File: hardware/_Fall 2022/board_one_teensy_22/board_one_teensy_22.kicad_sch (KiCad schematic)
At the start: 11 parts, among them J1 Conn_01x04, U1 Teensy4.1, U2 BNO055_Breakout, U3 MPL3115A2_Breakout

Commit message: Update main teensy board
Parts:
- added C1: 0.1uF, symbol Device:C
- R1, R2, R3: renamed from R?; value R -> 750
- gave numbers to parts that had none: 4
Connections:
- net GND: now also C1.2
- net Reg. 3.3 V renamed V_TEENSY
- net V_TEENSY: now also C1.1
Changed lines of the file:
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@@
+    (stroke (width 0) (type default) (color 0 0 0 0))
+  )
+  (wire (pts (xy 266.7 71.12) (xy 266.7 77.47))
     (stroke (width 0) (type default) (color 0 0 0 0))
   )
@@
     (stroke (width 0) (type default) (color 0 0 0 0))
   )
+  (wire (pts (xy 267.97 53.34) (xy 267.97 57.15))
+    (stroke (width 0) (type default) (color 0 0 0 0))
+  )
   (wire (pts (xy 88.9 180.34) (xy 100.33 180.34))
     (stroke (width 0) (type default) (color 0 0 0 0))
@@
     (stroke (width 0) (type default) (color 0 0 0 0))
   )
+  (wire (pts (xy 267.97 41.91) (xy 267.97 45.72))
+    (stroke (width 0) (type default) (color 0 0 0 0))
+  )
   (wire (pts (xy 22.86 35.56) (xy 35.56 35.56))
     (stroke (width 0) (type default) (color 0 0 0 0))
@@
     (effects (font (size 1.27 1.27)) (justify left bottom))
   )
+  (label "V_TEENSY" (at 267.97 41.91 0)
+    (effects (font (size 1.27 1.27)) (justify left bottom))
+  )
   (label "GND" (at 87.63 63.5 0)
     (effects (font (size 1.27 1.27)) (justify left bottom))
@@
     (effects (font (size 1.27 1.27)) (justify left bottom))
   )
-  (label "Reg. 3.3 V" (at 243.84 52.07 0)
+  (label "V_TEENSY" (at 243.84 52.07 0)
     (effects (font (size 1.27 1.27)) (justify left bottom))
   )
@@
   )
   (label "SCL0" (at 88.9 121.92 0)
+    (effects (font (size 1.27 1.27)) (justify left bottom))
+  )
+  (label "GND" (at 266.7 71.12 0)
     (effects (font (size 1.27 1.27)) (justify left bottom))
   )
@@
     (pin "4")
   )
+  (symbol (lib_id "power:GND") (at 266.7 77.47 0) (unit 1)
+    (in_bom yes) (on_board yes) (fields_autoplaced)
+    (property "Reference" "#PWR0102" (id 0) (at 266.7 83.82 0)
+      (effects (font (size 1.27 1.27)) hide)
+    )
+    (property "Value" "GND" (id 1) (at 266.7 82.55 0))
+    (property "Footprint" "" (id 2) (at 266.7 77.47 0)
+      (effects (font (size 1.27 1.27)) hide)
+    )
+    (property "Datasheet" "" (id 3) (at 266.7 77.47 0)
+      (effects (font (size 1.27 1.27)) hide)
+    )
+    (pin "1")
+  )
   (symbol (lib_id "REV2_SPRING_2022-rescue:MPL3115A2_Breakout-Sensors_2021_2022") (at 102.87 114.3 0) (unit 1)
     (in_bom yes) (on_board yes)
@@
   (symbol (lib_id "Connector:Conn_01x09_Female") (at 40.64 40.64 0) (unit 1)
     (in_bom yes) (on_board yes) (fields_autoplaced)
-    (property "Reference" "J?" (id 0) (at 41.91 39.3699 0)
+    (property "Reference" "J2" (id 0) (at 41.91 39.3699 0)
       (effects (font (size 1.27 1.27)) (justify left))
     )
@@
     (pin "9")
   )
+  (symbol (lib_id "power:GND") (at 267.97 57.15 0) (unit 1)
+    (in_bom yes) (on_board yes) (fields_autoplaced)
+    (property "Reference" "#PWR0101" (id 0) (at 267.97 63.5 0)
+      (effects (font (size 1.27 1.27)) hide)
+    )
+    (property "Value" "GND" (id 1) (at 267.97 62.23 0))
+    (property "Footprint" "" (id 2) (at 267.97 57.15 0)
+      (effects (font (size 1.27 1.27)) hide)
+    )
+    (property "Datasheet" "" (id 3) (at 267.97 57.15 0)
+      (effects (font (size 1.27 1.27)) hide)
+    )
+    (pin "1")
+  )
   (symbol (lib_id "Device:R") (at 85.09 157.48 90) (unit 1)
     (in_bom yes) (on_board yes) (fields_autoplaced)
-    (property "Reference" "R?" (id 0) (at 85.09 151.13 90))
-    (property "Value" "R" (id 1) (at 85.09 153.67 90))
+    (property "Reference" "R1" (id 0) (at 85.09 151.13 90))
+    (property "Value" "750" (id 1) (at 85.09 153.67 90))
     (property "Footprint" "" (id 2) (at 85.09 159.258 90)
       (effects (font (size 1.27 1.27)) hide)
@@
   (symbol (lib_id "Device:LED") (at 104.14 168.91 0) (unit 1)
     (in_bom yes) (on_board yes) (fields_autoplaced)
-    (property "Reference" "D?" (id 0) (at 102.5525 162.56 0))
+    (property "Reference" "D2" (id 0) (at 102.5525 162.56 0))
     (property "Value" "LED" (id 1) (at 102.5525 165.1 0))
     (property "Footprint" "" (id 2) (at 104.14 168.91 0)
@@
   (symbol (lib_id "Device:R") (at 85.09 180.34 90) (unit 1)
     (in_bom yes) (on_board yes) (fields_autoplaced)
-    (property "Reference" "R?" (id 0) (at 85.09 173.99 90))
-    (property "Value" "R" (id 1) (at 85.09 176.53 90))
+    (property "Reference" "R3" (id 0) (at 85.09 173.99 90))
+    (property "Value" "750" (id 1) (at 85.09 176.53 90))
     (property "Footprint" "" (id 2) (at 85.09 182.118 90)
       (effects (font (size 1.27 1.27)) hide)
@@
     (pin "4")
   )
+  (symbol (lib_id "Device:C") (at 267.97 49.53 0) (unit 1)
+    (in_bom yes) (on_board yes) (fields_autoplaced)
+    (property "Reference" "C1" (id 0) (at 271.78 48.2599 0)
+      (effects (font (size 1.27 1.27)) (justify left))
+    )
+    (property "Value" "0.1uF" (id 1) (at 271.78 50.7999 0)
+      (effects (font (size 1.27 1.27)) (justify left))
+    )
+    (property "Footprint" "" (id 2) (at 268.9352 53.34 0)
+      (effects (font (size 1.27 1.27)) hide)
+    )
+    (property "Datasheet" "~" (id 3) (at 267.97 49.53 0)
+      (effects (font (size 1.27 1.27)) hide)
+    )
+    (pin "1")
+    (pin "2")
+  )
   (symbol (lib_id "Device:LED") (at 104.14 180.34 0) (unit 1)
     (in_bom yes) (on_board yes) (fields_autoplaced)
-    (property "Reference" "D?" (id 0) (at 102.5525 173.99 0))
+    (property "Reference" "D3" (id 0) (at 102.5525 173.99 0))
     (property "Value" "LED" (id 1) (at 102.5525 176.53 0))
     (property "Footprint" "" (id 2) (at 104.14 180.34 0)
@@
   (symbol (lib_id "Device:LED") (at 104.14 157.48 0) (unit 1)
     (in_bom yes) (on_board yes) (fields_autoplaced)
-    (property "Reference" "D?" (id 0) (at 102.5525 151.13 0))
+    (property "Reference" "D1" (id 0) (at 102.5525 151.13 0))
     (property "Value" "LED" (id 1) (at 102.5525 153.67 0))
     (property "Footprint" "" (id 2) (at 104.14 157.48 0)
@@
   (symbol (lib_id "Device:R") (at 85.09 168.91 90) (unit 1)
     (in_bom yes) (on_board yes) (fields_autoplaced)
-    (property "Reference" "R?" (id 0) (at 85.09 162.56 90))
-    (property "Value" "R" (id 1) (at 85.09 165.1 90))
+    (property "Reference" "R2" (id 0) (at 85.09 162.56 90))
+    (property "Value" "750" (id 1) (at 85.09 165.1 90))
     (property "Footprint" "" (id 2) (at 85.09 170.688 90)
       (effects (font (size 1.27 1.27)) hide)
@@
   )
   (symbol_instances
+    (path "/8f40d9eb-5fdf-45db-bc50-610230c043b9"
+      (reference "#PWR0101") (unit 1) (value "GND") (footprint "")
+    )
+    (path "/46273ce1-7651-40e9-8fe5-ad122a75d0a7"
+      (reference "#PWR0102") (unit 1) (value "GND") (footprint "")
+    )
+    (path "/c535219e-946a-4ec5-bf45-7e1cca9e717d"
+      (reference "C1") (unit 1) (value "0.1uF") (footprint "")
+    )
+    (path "/e90f50d6-0a2f-4af0-9f06-35ce626c0dd6"
+      (reference "D1") (unit 1) (value "LED") (footprint "")
+    )
     (path "/ac0e113a-035a-46d2-97ae-1c57b8941c5b"
-      (reference "D?") (unit 1) (value "LED") (footprint "")
+      (reference "D2") (unit 1) (value "LED") (footprint "")
     )
     (path "/e2c8cf26-3d78-44d0-8af4-f027e582a996"
-      (reference "D?") (unit 1) (value "LED") (footprint "")
-    )
-    (path "/e90f50d6-0a2f-4af0-9f06-35ce626c0dd6"
-      (reference "D?") (unit 1) (value "LED") (footprint "")
+      (reference "D3") (unit 1) (value "LED") (footprint "")
     )
     (path "/c1ad9257-9aae-4dda-b1f1-b68d34349218"
@@
     )
     (path "/8786a6df-54d0-499d-9a7d-c5f993b94e72"
-      (reference "J?") (unit 1) (value "Conn_01x09_Female") (footprint "")
+      (reference "J2") (unit 1) (value "Conn_01x09_Female") (footprint "")
     )
     (path "/93bdb61a-71f4-45c4-b1f5-96e6332b02ef"
-      (reference "R?") (unit 1) (value "R") (footprint "")
+      (reference "R1") (unit 1) (value "750") (footprint "")
+    )
+    (path "/e9dd9e52-6e0d-4182-9ca4-63d8a2882b48"
+      (reference "R2") (unit 1) (value "750") (footprint "")
     )
     (path "/aca13756-ff3c-44cf-93bb-52afba450064"
-      (reference "R?") (unit 1) (value "R") (footprint "")
-    )
-    (path "/e9dd9e52-6e0d-4182-9ca4-63d8a2882b48"
-      (reference "R?") (unit 1) (value "R") (footprint "")
+      (reference "R3") (unit 1) (value "750") (footprint "")
     )
     (path "/1049841c-d8e6-470c-9b96-846caad7e784"

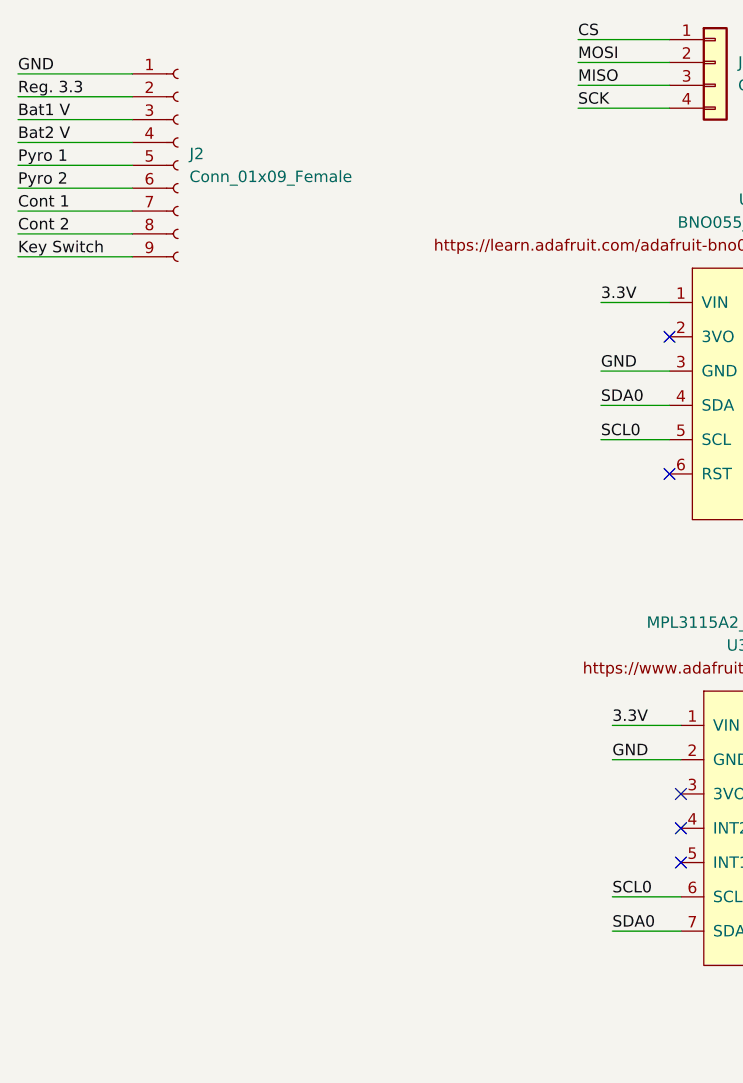
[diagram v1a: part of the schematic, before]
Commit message: Update schematics for both Teensy board schematics
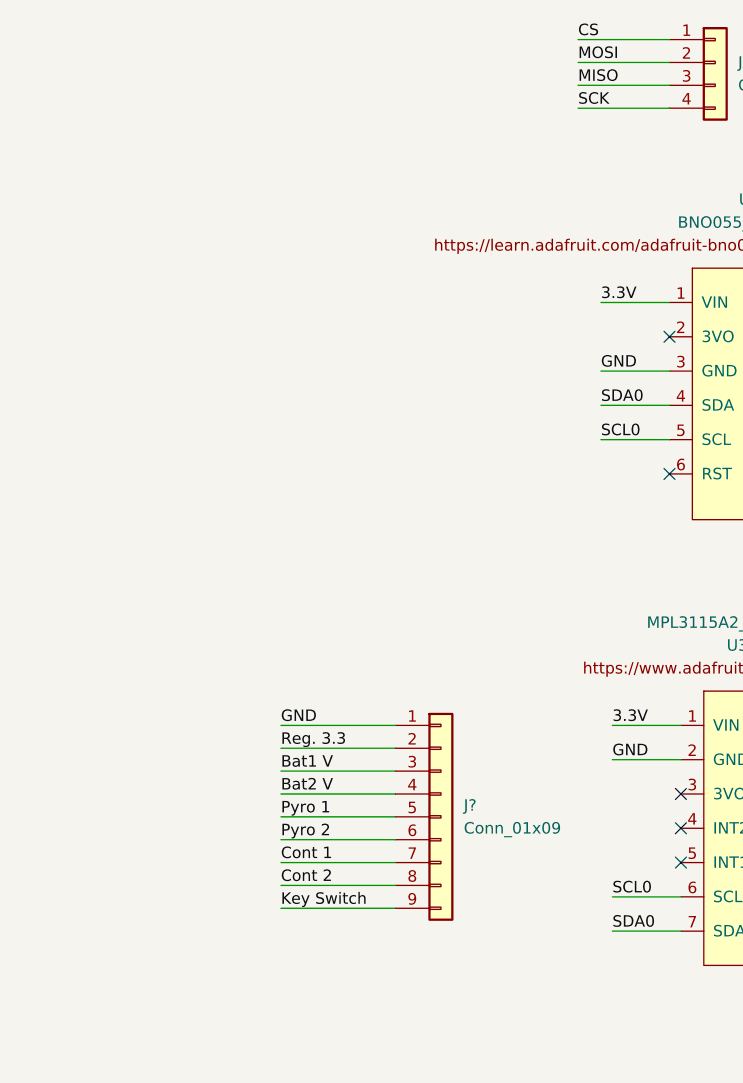
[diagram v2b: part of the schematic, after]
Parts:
- removed J2: Conn_01x09_Female, symbol Connector:Conn_01x09_Female
- added J?: Conn_01x09, symbol Connector_Generic:Conn_01x09
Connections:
- net Bat1 V: now also J?.3 (Pin_3)
- net Bat2 V: now also J?.4 (Pin_4)
- net Cont 1: now also J?.7 (Pin_7)
- net Cont 2: now also J?.8 (Pin_8)
- net GND: now also J?.1 (Pin_1)
- net Key Switch: now also J?.9 (Pin_9)
- net Pyro 1: now also J?.5 (Pin_5)
- net Pyro 2: now also J?.6 (Pin_6)
- net Reg. 3.3: now also J?.2 (Pin_2)
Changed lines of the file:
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@@
     (stroke (width 0) (type default) (color 0 0 0 0))
   )
-  (wire (pts (xy 22.86 40.64) (xy 35.56 40.64))
+  (wire (pts (xy 52.07 113.03) (xy 64.77 113.03))
     (stroke (width 0) (type default) (color 0 0 0 0))
   )
@@
     (stroke (width 0) (type default) (color 0 0 0 0))
   )
-  (wire (pts (xy 22.86 48.26) (xy 35.56 48.26))
+  (wire (pts (xy 52.07 120.65) (xy 64.77 120.65))
     (stroke (width 0) (type default) (color 0 0 0 0))
   )
@@
     (stroke (width 0) (type default) (color 0 0 0 0))
   )
-  (wire (pts (xy 22.86 30.48) (xy 35.56 30.48))
-    (stroke (width 0) (type default) (color 0 0 0 0))
-  )
-  (wire (pts (xy 22.86 50.8) (xy 35.56 50.8))
+  (wire (pts (xy 52.07 102.87) (xy 64.77 102.87))
+    (stroke (width 0) (type default) (color 0 0 0 0))
+  )
+  (wire (pts (xy 52.07 123.19) (xy 64.77 123.19))
     (stroke (width 0) (type default) (color 0 0 0 0))
   )
@@
     (stroke (width 0) (type default) (color 0 0 0 0))
   )
-  (wire (pts (xy 22.86 38.1) (xy 35.56 38.1))
+  (wire (pts (xy 52.07 110.49) (xy 64.77 110.49))
     (stroke (width 0) (type default) (color 0 0 0 0))
   )
@@
     (stroke (width 0) (type default) (color 0 0 0 0))
   )
-  (wire (pts (xy 22.86 43.18) (xy 35.56 43.18))
-    (stroke (width 0) (type default) (color 0 0 0 0))
-  )
-  (wire (pts (xy 22.86 45.72) (xy 35.56 45.72))
+  (wire (pts (xy 52.07 115.57) (xy 64.77 115.57))
+    (stroke (width 0) (type default) (color 0 0 0 0))
+  )
+  (wire (pts (xy 52.07 118.11) (xy 64.77 118.11))
     (stroke (width 0) (type default) (color 0 0 0 0))
   )
@@
     (stroke (width 0) (type default) (color 0 0 0 0))
   )
-  (wire (pts (xy 22.86 33.02) (xy 35.56 33.02))
+  (wire (pts (xy 52.07 105.41) (xy 64.77 105.41))
     (stroke (width 0) (type default) (color 0 0 0 0))
   )
@@
     (stroke (width 0) (type default) (color 0 0 0 0))
   )
-  (wire (pts (xy 22.86 35.56) (xy 35.56 35.56))
+  (wire (pts (xy 52.07 107.95) (xy 64.77 107.95))
     (stroke (width 0) (type default) (color 0 0 0 0))
   )
@@
     (effects (font (size 1.27 1.27)) (justify left bottom))
   )
-  (label "Bat1 V" (at 22.86 35.56 0)
+  (label "Bat1 V" (at 52.07 107.95 0)
     (effects (font (size 1.27 1.27)) (justify left bottom))
   )
@@
     (effects (font (size 1.27 1.27)) (justify left bottom))
   )
-  (label "Pyro 2" (at 22.86 43.18 0)
+  (label "Pyro 2" (at 52.07 115.57 0)
     (effects (font (size 1.27 1.27)) (justify left bottom))
   )
@@
     (effects (font (size 1.27 1.27)) (justify left bottom))
   )
-  (label "Reg. 3.3" (at 22.86 33.02 0)
+  (label "Reg. 3.3" (at 52.07 105.41 0)
     (effects (font (size 1.27 1.27)) (justify left bottom))
   )
@@
     (effects (font (size 1.27 1.27)) (justify left bottom))
   )
-  (label "Bat2 V" (at 22.86 38.1 0)
+  (label "Bat2 V" (at 52.07 110.49 0)
     (effects (font (size 1.27 1.27)) (justify left bottom))
   )
@@
     (effects (font (size 1.27 1.27)) (justify left bottom))
   )
-  (label "Key Switch" (at 22.86 50.8 0)
+  (label "Key Switch" (at 52.07 123.19 0)
     (effects (font (size 1.27 1.27)) (justify left bottom))
   )
@@
     (effects (font (size 1.27 1.27)) (justify left bottom))
   )
-  (label "Cont 2" (at 22.86 48.26 0)
+  (label "Cont 2" (at 52.07 120.65 0)
     (effects (font (size 1.27 1.27)) (justify left bottom))
   )
@@
     (effects (font (size 1.27 1.27)) (justify left bottom))
   )
-  (label "Cont 1" (at 22.86 45.72 0)
+  (label "Cont 1" (at 52.07 118.11 0)
     (effects (font (size 1.27 1.27)) (justify left bottom))
   )
@@
     (effects (font (size 1.27 1.27)) (justify left bottom))
   )
-  (label "Pyro 1" (at 22.86 40.64 0)
+  (label "Pyro 1" (at 52.07 113.03 0)
     (effects (font (size 1.27 1.27)) (justify left bottom))
   )
@@
     (effects (font (size 1.27 1.27)) (justify left bottom))
   )
-  (label "GND" (at 22.86 30.48 0)
+  (label "GND" (at 52.07 102.87 0)
     (effects (font (size 1.27 1.27)) (justify left bottom))
   )
@@
     (pin "7")
   )
-  (symbol (lib_id "Connector:Conn_01x09_Female") (at 40.64 40.64 0) (unit 1)
-    (in_bom yes) (on_board yes) (fields_autoplaced)
-    (property "Reference" "J2" (id 0) (at 41.91 39.3699 0)
-      (effects (font (size 1.27 1.27)) (justify left))
-    )
-    (property "Value" "Conn_01x09_Female" (id 1) (at 41.91 41.9099 0)
-      (effects (font (size 1.27 1.27)) (justify left))
-    )
-    (property "Footprint" "" (id 2) (at 40.64 40.64 0)
-      (effects (font (size 1.27 1.27)) hide)
-    )
-    (property "Datasheet" "~" (id 3) (at 40.64 40.64 0)
+  (symbol (lib_id "Connector_Generic:Conn_01x09") (at 69.85 113.03 0) (unit 1)
+    (in_bom yes) (on_board yes) (fields_autoplaced)
+    (property "Reference" "J?" (id 0) (at 72.39 111.7599 0)
+      (effects (font (size 1.27 1.27)) (justify left))
+    )
+    (property "Value" "Conn_01x09" (id 1) (at 72.39 114.2999 0)
+      (effects (font (size 1.27 1.27)) (justify left))
+    )
+    (property "Footprint" "" (id 2) (at 69.85 113.03 0)
+      (effects (font (size 1.27 1.27)) hide)
+    )
+    (property "Datasheet" "~" (id 3) (at 69.85 113.03 0)
       (effects (font (size 1.27 1.27)) hide)
     )
@@
       (reference "J1") (unit 1) (value "Conn_01x04") (footprint "")
     )
-    (path "/8786a6df-54d0-499d-9a7d-c5f993b94e72"
-      (reference "J2") (unit 1) (value "Conn_01x09_Female") (footprint "")
+    (path "/7b090083-bf94-4a7a-b7fa-997eaeb1d5a8"
+      (reference "J?") (unit 1) (value "Conn_01x09") (footprint "")
     )
     (path "/93bdb61a-71f4-45c4-b1f5-96e6332b02ef"
